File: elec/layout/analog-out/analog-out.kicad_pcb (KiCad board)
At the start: 2 copper layers, 8 parts, among them U1 10kΩ ±1% 62.5mW, U2 10kΩ ±1% 62.5mW, U3 BW CMRR Ib Vos GBW Iout SR, U5 100nF ±10% 50V X7R, U6 100kΩ ±1% 62.5mW, U7 1µF ±10% 25V X5R

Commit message: build and re-link layouts
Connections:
- D1 pad 1: line-2 -> line
- U1 pad 2: line-2 -> line
- U3 pad 1: line-2 -> line
- U4 pad 5: line -> line-2
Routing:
- net line-2: track 11.6 -> 0.00 mm
- net line: track 0.00 -> 11.6 mm
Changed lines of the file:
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@@
     (net 3 "amplifier.opamp.footprint.pins[5].net-net")
     (net 4 "non_inverting_input")
-    (net 5 "line")
+    (net 5 "line-2")
     (net 6 "gnd-1")
     (net 7 "line-1")
@@
     (net 9 "amplifier.opamp.footprint.pins[4].net-net")
     (net 10 "hv")
-    (net 11 "line-2")
+    (net 11 "line")
     (net 12 "hv-1")
     (footprint "atopile:SMB_L4.6-W3.6-LS5.3-RD-330cb3"
@@
             (layers "F.Cu" "F.Paste" "F.Mask")
             (remove_unused_layers no)
-            (net 11 "line-2"))
+            (net 11 "line"))
         (pad "2" smd rect
             (at 2.36 0 270)
@@
             (layers "F.Cu" "F.Paste" "F.Mask")
             (remove_unused_layers no)
-            (net 11 "line-2")))
+            (net 11 "line")))
     (footprint "atopile:C0402-b3ef17"
         (layer "F.Cu")
@@
             (layers "F.Cu" "F.Paste" "F.Mask")
             (remove_unused_layers no)
-            (net 5 "line"))
+            (net 5 "line-2"))
         (pad "6" smd rect
             (at -0.95 -1.15 90)
@@
             (layers "F.Cu" "F.Paste" "F.Mask")
             (remove_unused_layers no)
-            (net 11 "line-2"))
+            (net 11 "line"))
         (pad "2" smd oval
             (at -0.63 2.71 270)

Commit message: all modules building
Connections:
- net gnd-1 renamed gnd
- D1 pad 1: line -> line-1
- U1 pad 2: line -> line-1
- U3 pad 1: line -> line-1
- U3 pad 8: hv-1 -> hv
- U4 pad 1: line-1 -> line-2
- U4 pad 3: hv -> hv-1
- U4 pad 4: line-3 -> line
- U4 pad 5: line-2 -> line-3
- U6 pad 1: line-1 -> line-2
- U7 pad 1: hv-1 -> hv
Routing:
- net line: track 11.6 -> 0.00 mm
- net line-1: track 1.94 -> 11.6 mm
- net line-2: track 0.00 -> 1.94 mm
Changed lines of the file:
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@@
             (outputdirectory "")))
     (net 0 "")
-    (net 1 "line-3")
+    (net 1 "line")
     (net 2 "amplifier.opamp.footprint.pins[6].net-net")
     (net 3 "amplifier.opamp.footprint.pins[5].net-net")
     (net 4 "non_inverting_input")
-    (net 5 "line-2")
-    (net 6 "gnd-1")
-    (net 7 "line-1")
+    (net 5 "line-3")
+    (net 6 "gnd")
+    (net 7 "line-2")
     (net 8 "inverting_input")
     (net 9 "amplifier.opamp.footprint.pins[4].net-net")
-    (net 10 "hv")
-    (net 11 "line")
-    (net 12 "hv-1")
+    (net 10 "hv-1")
+    (net 11 "line-1")
+    (net 12 "hv")
     (footprint "atopile:SMB_L4.6-W3.6-LS5.3-RD-330cb3"
         (layer "F.Cu")
@@
             (layers "F.Cu" "F.Paste" "F.Mask")
             (remove_unused_layers no)
-            (net 11 "line"))
+            (net 11 "line-1"))
         (pad "2" smd rect
             (at 2.36 0 270)
@@
             (layers "F.Cu" "F.Paste" "F.Mask")
             (remove_unused_layers no)
-            (net 6 "gnd-1")))
+            (net 6 "gnd")))
     (footprint "atopile:R0402-56259e"
         (layer "F.Cu")
@@
             (layers "F.Cu" "F.Paste" "F.Mask")
             (remove_unused_layers no)
-            (net 7 "line-1")))
+            (net 7 "line-2")))
     (footprint "atopile:R0402-56259e"
         (layer "F.Cu")
@@
             (layers "F.Cu" "F.Paste" "F.Mask")
             (remove_unused_layers no)
-            (net 11 "line")))
+            (net 11 "line-1")))
     (footprint "atopile:C0402-b3ef17"
         (layer "F.Cu")
@@
             (layers "F.Cu" "F.Paste" "F.Mask")
             (remove_unused_layers no)
-            (net 12 "hv-1"))
+            (net 12 "hv"))
         (pad "2" smd rect
             (at 0.55 0 180)
@@
             (layers "F.Cu" "F.Paste" "F.Mask")
             (remove_unused_layers no)
-            (net 6 "gnd-1")))
+            (net 6 "gnd")))
     (footprint "lib:SOT-23-6_L2.9-W1.6-P0.95-LS2.8-BL"
         (layer "F.Cu")
@@
             (layers "F.Cu" "F.Paste" "F.Mask")
             (remove_unused_layers no)
-            (net 7 "line-1"))
+            (net 7 "line-2"))
         (pad "2" smd rect
             (at 0 1.15 90)
@@
             (layers "F.Cu" "F.Paste" "F.Mask")
             (remove_unused_layers no)
-            (net 6 "gnd-1"))
+            (net 6 "gnd"))
         (pad "3" smd rect
             (at 0.95 1.15 90)
@@
             (layers "F.Cu" "F.Paste" "F.Mask")
             (remove_unused_layers no)
-            (net 10 "hv"))
+            (net 10 "hv-1"))
         (pad "4" smd rect
             (at 0.95 -1.15 90)
@@
             (layers "F.Cu" "F.Paste" "F.Mask")
             (remove_unused_layers no)
-            (net 1 "line-3"))
+            (net 1 "line"))
         (pad "5" smd rect
             (at 0 -1.15 90)
@@
             (layers "F.Cu" "F.Paste" "F.Mask")
             (remove_unused_layers no)
-            (net 5 "line-2"))
+            (net 5 "line-3"))
         (pad "6" smd rect
             (at -0.95 -1.15 90)
@@
             (layers "F.Cu" "F.Paste" "F.Mask")
             (remove_unused_layers no)
-            (net 6 "gnd-1"))
+            (net 6 "gnd"))
         (model "/Users/narayanpowderly/projects/hil-blocks/build/footprints/footprints.3dshapes/SOT-23-6_L2.9-W1.6-H1.5-LS2.8-P0.95.step"
             (offset
@@
             (layers "F.Cu" "F.Paste" "F.Mask")
             (remove_unused_layers no)
-            (net 6 "gnd-1")))
+            (net 6 "gnd")))
     (footprint "atopile:SOIC-8_L5.0-W4.0-P1.27-LS6.0-BL-294f77"
         (layer "F.Cu")
@@
             (layers "F.Cu" "F.Paste" "F.Mask")
             (remove_unused_layers no)
-            (net 11 "line"))
+            (net 11 "line-1"))
         (pad "2" smd oval
             (at -0.63 2.71 270)
@@
             (layers "F.Cu" "F.Paste" "F.Mask")
             (remove_unused_layers no)
-            (net 6 "gnd-1"))
+            (net 6 "gnd"))
         (pad "5" smd oval
             (at 1.9 -2.71 270)
@@
             (layers "F.Cu" "F.Paste" "F.Mask")
             (remove_unused_layers no)
-            (net 12 "hv-1")))
+            (net 12 "hv")))
     (footprint "atopile:R0402-56259e"
         (layer "F.Cu")
@@
             (layers "F.Cu" "F.Paste" "F.Mask")
             (remove_unused_layers no)
-            (net 6 "gnd-1"))
+            (net 6 "gnd"))
         (pad "2" smd rect
             (at 0.43 0 0)

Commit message: HIL Building
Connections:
- net gnd renamed dac-line
- U3 pad 8: hv -> hv-1
- U4 pad 1: line-2 -> line
- U4 pad 3: hv-1 -> hv
- U4 pad 4: line -> line-2
- U6 pad 1: line-2 -> line
- U7 pad 1: hv -> hv-1
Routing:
- net line-2: track 1.94 -> 0.00 mm
- net line: track 0.00 -> 1.94 mm
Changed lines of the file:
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@@
             (outputdirectory "")))
     (net 0 "")
-    (net 1 "line")
+    (net 1 "line-2")
     (net 2 "amplifier.opamp.footprint.pins[6].net-net")
     (net 3 "amplifier.opamp.footprint.pins[5].net-net")
     (net 4 "non_inverting_input")
     (net 5 "line-3")
-    (net 6 "gnd")
-    (net 7 "line-2")
+    (net 6 "dac-line")
+    (net 7 "line")
     (net 8 "inverting_input")
     (net 9 "amplifier.opamp.footprint.pins[4].net-net")
-    (net 10 "hv-1")
+    (net 10 "hv")
     (net 11 "line-1")
-    (net 12 "hv")
+    (net 12 "hv-1")
     (footprint "atopile:SMB_L4.6-W3.6-LS5.3-RD-330cb3"
         (layer "F.Cu")
@@
             (layers "F.Cu" "F.Paste" "F.Mask")
             (remove_unused_layers no)
-            (net 6 "gnd")))
+            (net 6 "dac-line")))
     (footprint "atopile:R0402-56259e"
         (layer "F.Cu")
@@
             (layers "F.Cu" "F.Paste" "F.Mask")
             (remove_unused_layers no)
-            (net 7 "line-2")))
+            (net 7 "line")))
     (footprint "atopile:R0402-56259e"
         (layer "F.Cu")
@@
             (layers "F.Cu" "F.Paste" "F.Mask")
             (remove_unused_layers no)
-            (net 12 "hv"))
+            (net 12 "hv-1"))
         (pad "2" smd rect
             (at 0.55 0 180)
@@
             (layers "F.Cu" "F.Paste" "F.Mask")
             (remove_unused_layers no)
-            (net 6 "gnd")))
+            (net 6 "dac-line")))
     (footprint "lib:SOT-23-6_L2.9-W1.6-P0.95-LS2.8-BL"
         (layer "F.Cu")
@@
             (layers "F.Cu" "F.Paste" "F.Mask")
             (remove_unused_layers no)
-            (net 7 "line-2"))
+            (net 7 "line"))
         (pad "2" smd rect
             (at 0 1.15 90)
@@
             (layers "F.Cu" "F.Paste" "F.Mask")
             (remove_unused_layers no)
-            (net 6 "gnd"))
+            (net 6 "dac-line"))
         (pad "3" smd rect
             (at 0.95 1.15 90)
@@
             (layers "F.Cu" "F.Paste" "F.Mask")
             (remove_unused_layers no)
-            (net 10 "hv-1"))
+            (net 10 "hv"))
         (pad "4" smd rect
             (at 0.95 -1.15 90)
@@
             (layers "F.Cu" "F.Paste" "F.Mask")
             (remove_unused_layers no)
-            (net 1 "line"))
+            (net 1 "line-2"))
         (pad "5" smd rect
             (at 0 -1.15 90)
@@
             (layers "F.Cu" "F.Paste" "F.Mask")
             (remove_unused_layers no)
-            (net 6 "gnd"))
+            (net 6 "dac-line"))
         (model "/Users/narayanpowderly/projects/hil-blocks/build/footprints/footprints.3dshapes/SOT-23-6_L2.9-W1.6-H1.5-LS2.8-P0.95.step"
             (offset
@@
             (layers "F.Cu" "F.Paste" "F.Mask")
             (remove_unused_layers no)
-            (net 6 "gnd")))
+            (net 6 "dac-line")))
     (footprint "atopile:SOIC-8_L5.0-W4.0-P1.27-LS6.0-BL-294f77"
         (layer "F.Cu")
@@
             (layers "F.Cu" "F.Paste" "F.Mask")
             (remove_unused_layers no)
-            (net 6 "gnd"))
+            (net 6 "dac-line"))
         (pad "5" smd oval
             (at 1.9 -2.71 270)
@@
             (layers "F.Cu" "F.Paste" "F.Mask")
             (remove_unused_layers no)
-            (net 12 "hv")))
+            (net 12 "hv-1")))
     (footprint "atopile:R0402-56259e"
         (layer "F.Cu")
@@
             (layers "F.Cu" "F.Paste" "F.Mask")
             (remove_unused_layers no)
-            (net 6 "gnd"))
+            (net 6 "dac-line"))
         (pad "2" smd rect
             (at 0.43 0 0)

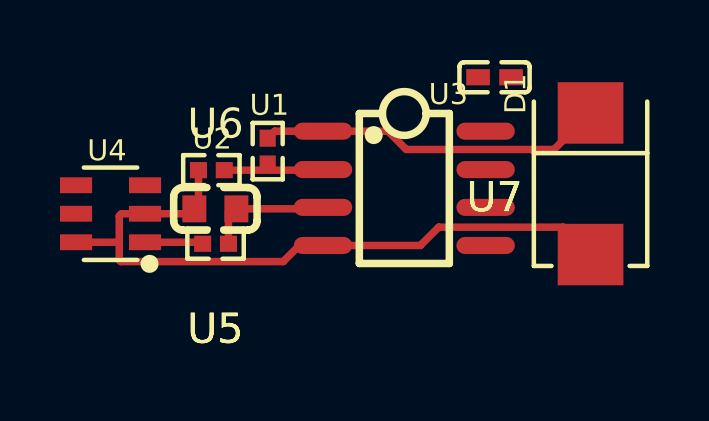
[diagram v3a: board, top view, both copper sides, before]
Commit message: Fix address bit issue, update layouts
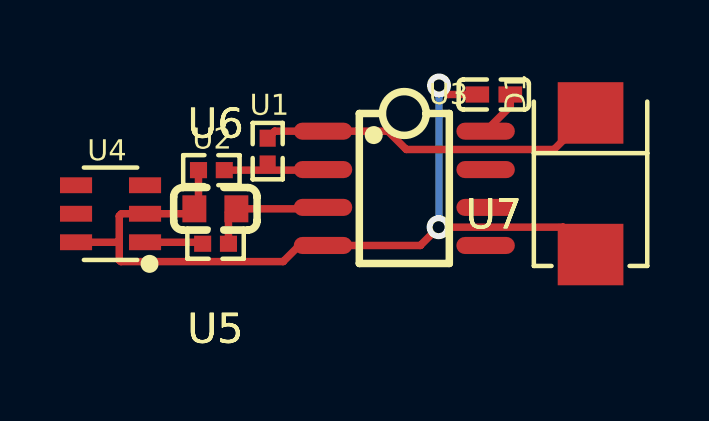
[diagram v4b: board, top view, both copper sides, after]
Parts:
- moved U7 0.58 mm to (148.8, 86.0)
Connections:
- D1 pad 2: dac-line -> gnd
- U2 pad 1: dac-line -> gnd
- U3 pad 4: dac-line -> gnd
- U4 pad 1: line -> line-2
- U4 pad 2: dac-line -> gnd-1
- U4 pad 4: line-2 -> line-3
- U4 pad 5: line-3 -> line
- U4 pad 6: dac-line -> gnd
- U5 pad 2: dac-line -> gnd-1
- U6 pad 1: line -> line-2
- U7 pad 2: dac-line -> gnd
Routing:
- net gnd: track 0.00 -> 29.7 mm, vias 0 -> 2
- net dac-line: track 23.6 -> 0.00 mm
- net line-2: track 0.00 -> 1.94 mm
- net line: track 1.94 -> 0.00 mm
- net hv-1: track 0.00 -> 1.56 mm

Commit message: build with latest main
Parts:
- removed D1: , atopile:SMB_L4.6-W3.6-LS5.3-RD-330cb3
- removed U1, U2: 10kΩ ±1% 62.5mW, atopile:R0402-56259e
- removed U3: BW CMRR Ib Vos GBW Iout SR, atopile:SOIC-8_L5.0-W4.0-P1.27-LS6.0-BL-294f77
- removed U4: , lib:SOT-23-6_L2.9-W1.6-P0.95-LS2.8-BL
- removed U5: 100nF ±10% 50V X7R, atopile:C0603-bd72f6
- removed U6: 100kΩ ±1% 62.5mW, atopile:R0402-56259e
- removed U7: 1µF ±10% 25V X5R, atopile:C0402-b3ef17
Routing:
- net gnd: track 29.7 -> 0.00 mm, vias 2 -> 0
- net line-1: track 11.6 -> 0.00 mm
- net non_inverting_input: track 4.27 -> 0.00 mm
- net inverting_input: track 3.30 -> 0.00 mm
- net line-2: track 1.94 -> 0.00 mm
- net hv-1: track 1.56 -> 0.00 mm
